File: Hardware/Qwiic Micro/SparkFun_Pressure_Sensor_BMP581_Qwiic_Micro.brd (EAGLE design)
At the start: 7.6 x 19.1 mm, 39 parts, among them J1 QWIIC_RIGHT_ANGLE, U1 BMP581

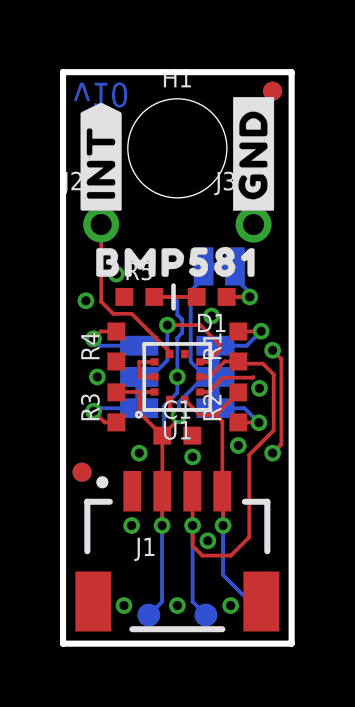
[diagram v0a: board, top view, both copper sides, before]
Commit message: Connect CSB of Micro board to VDD
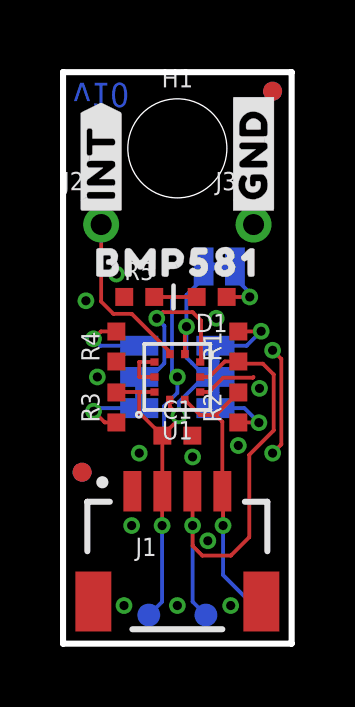
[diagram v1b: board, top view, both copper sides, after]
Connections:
- removed net !CSB!: U1.6
- net VDD: now also U1.6
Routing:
- net VDD: track 17.2 -> 18.2 mm, vias 2 -> 3
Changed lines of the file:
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@@
 <drawing>
 <settings>
-<setting alwaysvectorfont="yes"/>
+<setting alwaysvectorfont="no"/>
 <setting verticaltext="up"/>
 </settings>
@@
 <wire x1="5.08" y1="8.89" x2="4.699" y2="8.89" width="0.127" layer="16"/>
 <wire x1="5.08" y1="8.89" x2="4.759796875" y2="8.89" width="0.127" layer="16"/>
-<wire x1="4.759796875" y1="8.89" x2="4.2545" y2="9.39529375" width="0.127" layer="16"/>
-<wire x1="4.2545" y1="9.39529375" x2="4.2545" y2="11.7602" width="0.127" layer="16"/>
-<wire x1="4.6863" y1="12.192" x2="4.2545" y2="11.7602" width="0.127" layer="16"/>
+<wire x1="4.759796875" y1="8.89" x2="4.284896875" y2="9.364896875" width="0.127" layer="16"/>
 <wire x1="4.6863" y1="12.192" x2="4.6863" y2="12.573" width="0.127" layer="16"/>
+<via x="4.1148" y="10.5664" extent="1-16" drill="0.3048"/>
+<wire x1="4.06" y1="10.5116" x2="4.1148" y2="10.5664" width="0.127" layer="1"/>
+<wire x1="4.284896875" y1="9.364896875" x2="4.1148" y2="9.53499375" width="0.127" layer="16"/>
+<wire x1="4.1148" y1="9.53499375" x2="4.1148" y2="10.5664" width="0.127" layer="16"/>
+<wire x1="4.1148" y1="10.5664" x2="4.1148" y2="11.6205" width="0.127" layer="16"/>
+<wire x1="4.1148" y1="11.6205" x2="4.6863" y2="12.192" width="0.127" layer="16"/>
+<contactref element="U1" pad="6"/>
 <wire x1="3.0475" y1="8.39" x2="2.54" y2="8.39" width="0.127" layer="1"/>
 <wire x1="3.56" y1="8.1275" x2="3.56" y2="7.8954" width="0.127" layer="1"/>
+<wire x1="4.06" y1="9.6525" x2="4.06" y2="10.5116" width="0.127" layer="1"/>
 </signal>
 <signal name="GND">
@@
 <contactref element="C1" pad="2"/>
 <contactref element="R4" pad="1"/>
+<polygon width="0.254" layer="1" isolate="0.127">
+<vertex x="0" y="0"/>
+<vertex x="7.62" y="0"/>
+<vertex x="7.62" y="19.05"/>
+<vertex x="0" y="19.05"/>
+</polygon>
+<polygon width="0.254" layer="16" isolate="0.127">
+<vertex x="0" y="0"/>
+<vertex x="7.62" y="0"/>
+<vertex x="7.62" y="19.05"/>
+<vertex x="0" y="19.05"/>
+</polygon>
 <wire x1="1.0369" y1="0.9525" x2="0.9525" y2="0.9525" width="0.127" layer="16"/>
-<wire x1="2.54" y1="9.39" x2="2.54" y2="8.89" width="0.127" layer="1"/>
+<wire x1="2.54" y1="8.89" x2="2.54" y2="9.39" width="0.127" layer="1"/>
 <wire x1="6.3245" y1="8.8645" x2="6.35" y2="8.89" width="0.127" layer="1"/>
 <wire x1="4.86159375" y1="8.39" x2="5.33609375" y2="8.8645" width="0.127" layer="1"/>
@@
 <via x="0.762" y="11.43" extent="1-16" drill="0.3048"/>
 <via x="3.81" y="8.89" extent="1-16" drill="0.3048"/>
-<wire x1="3.81" y1="8.89" x2="3.81" y2="10.19404375" width="0.127" layer="16"/>
-<wire x1="3.81" y1="10.19404375" x2="3.9735" y2="10.35754375" width="0.127" layer="16"/>
-<wire x1="3.9735" y1="10.35754375" x2="3.9735" y2="10.80065625" width="0.127" layer="16"/>
-<wire x1="3.9735" y1="10.80065625" x2="3.81" y2="10.96415625" width="0.127" layer="16"/>
-<wire x1="3.81" y1="10.96415625" x2="3.81" y2="11.43" width="0.127" layer="16"/>
+<wire x1="3.81" y1="8.89" x2="3.6322" y2="9.0678" width="0.127" layer="16"/>
+<wire x1="3.6322" y1="11.4554" x2="3.6322" y2="9.0678" width="0.127" layer="16"/>
 <wire x1="3.81" y1="8.89" x2="3.81" y2="8.3602125" width="0.127" layer="16"/>
 <wire x1="3.3671" y1="7.0501" x2="3.302" y2="6.985" width="0.127" layer="16"/>
@@
 <via x="2.54" y="6.35" extent="1-16" drill="0.3048"/>
 <via x="1.143" y="8.89" extent="1-16" drill="0.3048"/>
-<via x="4.953" y="10.922" extent="1-16" drill="0.3048"/>
-<polygon width="0.254" layer="1" isolate="0.127">
-<vertex x="0" y="0"/>
-<vertex x="7.62" y="0"/>
-<vertex x="7.62" y="19.05"/>
-<vertex x="0" y="19.05"/>
-</polygon>
-<polygon width="0.254" layer="16" isolate="0.127">
-<vertex x="0" y="0"/>
-<vertex x="7.62" y="0"/>
-<vertex x="7.62" y="19.05"/>
-<vertex x="0" y="19.05"/>
-</polygon>
+<via x="5.1054" y="10.8458" extent="1-16" drill="0.3048"/>
 <wire x1="6.985" y1="6.35" x2="7.2771" y2="6.6421" width="0.127" layer="1"/>
 <wire x1="7.2771" y1="9.4869" x2="6.985" y2="9.779" width="0.127" layer="1"/>
 <wire x1="7.2771" y1="6.6421" x2="7.2771" y2="9.4869" width="0.127" layer="1"/>
+<wire x1="3.0475" y1="9.39" x2="2.54" y2="9.39" width="0.127" layer="1"/>
+<wire x1="3.0475" y1="8.89" x2="2.54" y2="8.89" width="0.127" layer="1"/>
 <wire x1="4.5725" y1="8.39" x2="4.86159375" y2="8.39" width="0.127" layer="1"/>
-<wire x1="3.0475" y1="8.89" x2="2.54" y2="8.89" width="0.127" layer="1"/>
-<wire x1="3.0475" y1="9.39" x2="2.54" y2="9.39" width="0.127" layer="1"/>
 </signal>
 <signal name="SDI/SDA">
@@
 <wire x1="5.334" y1="3.937" x2="5.334" y2="2.286" width="0.127" layer="16"/>
 <wire x1="5.334" y1="2.286" x2="6.6675" y2="0.9525" width="0.127" layer="16"/>
-<wire x1="4.06" y1="8.1275" x2="4.5675" y2="7.62" width="0.127" layer="1"/>
 <wire x1="4.5675" y1="7.62" x2="5.088" y2="7.62" width="0.127" layer="1"/>
+<wire x1="4.5675" y1="7.625" x2="4.5675" y2="7.62" width="0.127" layer="1"/>
+<wire x1="4.06" y1="8.1275" x2="4.5625" y2="7.625" width="0.127" layer="1"/>
+<wire x1="4.5625" y1="7.625" x2="4.5675" y2="7.625" width="0.127" layer="1"/>
 </signal>
 <signal name="SDO/ADR">
 <contactref element="U1" pad="5"/>
 <contactref element="JP1" pad="2"/>
-<via x="3.4798" y="10.6172" extent="1-16" drill="0.3048"/>
-<wire x1="3.4798" y1="10.6172" x2="4.572" y2="10.6172" width="0.127" layer="1"/>
-<wire x1="4.572" y1="10.6172" x2="5.207" y2="9.9822" width="0.127" layer="1"/>
-<wire x1="5.207" y1="9.9822" x2="5.207" y2="9.7755" width="0.127" layer="1"/>
-<wire x1="4.8215" y1="9.39" x2="5.207" y2="9.7755" width="0.127" layer="1"/>
+<via x="3.1242" y="10.8458" extent="1-16" drill="0.3048"/>
+<wire x1="3.1242" y1="10.8458" x2="3.3274" y2="11.049" width="0.127" layer="1"/>
+<wire x1="4.318" y1="11.049" x2="3.3274" y2="11.049" width="0.127" layer="1"/>
+<wire x1="4.5974" y1="10.7696" x2="4.318" y2="11.049" width="0.127" layer="1"/>
 <wire x1="2.54" y1="8.89" x2="2.921" y2="8.89" width="0.127" layer="16"/>
-<wire x1="2.921" y1="8.89" x2="3.4798" y2="9.4488" width="0.127" layer="16"/>
-<wire x1="3.4798" y1="9.4488" x2="3.4798" y2="10.6172" width="0.127" layer="16"/>
-<wire x1="4.5725" y1="9.39" x2="4.8215" y2="9.39" width="0.127" layer="1"/>
+<wire x1="2.921" y1="8.89" x2="3.3782" y2="9.3472" width="0.127" layer="16"/>
+<wire x1="3.3782" y1="10.5918" x2="3.1242" y2="10.8458" width="0.127" layer="16"/>
+<wire x1="3.3782" y1="10.5918" x2="3.3782" y2="9.3472" width="0.127" layer="16"/>
+<wire x1="4.5725" y1="9.39" x2="4.5974" y2="9.4149" width="0.127" layer="1"/>
+<wire x1="4.5974" y1="9.4149" x2="4.5974" y2="10.7696" width="0.127" layer="1"/>
 </signal>
 <signal name="INT">
@@
 <wire x1="3.56" y1="9.6525" x2="3.56" y2="9.7237" width="0.127" layer="1"/>
 </signal>
-<signal name="!CSB!">
-<contactref element="U1" pad="6"/>
-</signal>
 <signal name="N$5">

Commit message: Design review updates
Change INT label to fishtail in Micro silk
Add product name to bottom in 1x1 silk
Change Micro net labels to be I2C only
Approve DRC overlaps
Fix acid trap
Add note about CSB being tied high in Micro schematic
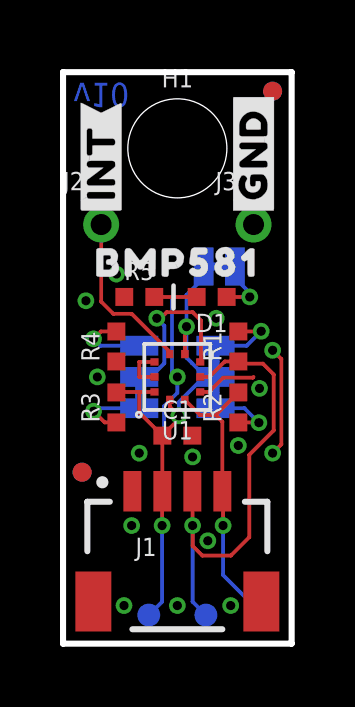
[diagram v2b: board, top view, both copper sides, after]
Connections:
- net SCK/SCL renamed SCL
- net SDI/SDA renamed SDA
- net SDO/ADR renamed ADR
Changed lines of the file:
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@@
 <drawing>
 <settings>
-<setting alwaysvectorfont="no"/>
+<setting alwaysvectorfont="yes"/>
 <setting verticaltext="up"/>
 </settings>
@@
 <wire x1="4.5725" y1="8.39" x2="4.86159375" y2="8.39" width="0.127" layer="1"/>
 </signal>
-<signal name="SDI/SDA">
+<signal name="SDA">
 <contactref element="U1" pad="4"/>
 <contactref element="J1" pad="3"/>
@@
 <wire x1="4.5725" y1="8.89" x2="4.87538125" y2="8.89" width="0.127" layer="1"/>
 </signal>
-<signal name="SCK/SCL">
+<signal name="SCL">
 <contactref element="U1" pad="2"/>
 <contactref element="J1" pad="4"/>
@@
 <wire x1="4.5625" y1="7.625" x2="4.5675" y2="7.625" width="0.127" layer="1"/>
 </signal>
-<signal name="SDO/ADR">
+<signal name="ADR">
 <contactref element="U1" pad="5"/>
 <contactref element="JP1" pad="2"/>
 <via x="3.1242" y="10.8458" extent="1-16" drill="0.3048"/>
-<wire x1="3.1242" y1="10.8458" x2="3.3274" y2="11.049" width="0.127" layer="1"/>
-<wire x1="4.318" y1="11.049" x2="3.3274" y2="11.049" width="0.127" layer="1"/>
+<wire x1="3.1242" y1="10.8458" x2="3.2512" y2="10.8458" width="0.127" layer="1"/>
+<wire x1="3.4544" y1="11.049" x2="3.2512" y2="10.8458" width="0.127" layer="1"/>
+<wire x1="4.318" y1="11.049" x2="3.4544" y2="11.049" width="0.127" layer="1"/>
 <wire x1="4.5974" y1="10.7696" x2="4.318" y2="11.049" width="0.127" layer="1"/>
 <wire x1="2.54" y1="8.89" x2="2.921" y2="8.89" width="0.127" layer="16"/>

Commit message: Remove library file
BMP384 is in SFE Eagle library, update part in design
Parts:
- U1: device BMP581:BMP581 -> SparkFun-Sensors:BMP581
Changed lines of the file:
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@@
 <element name="TP3" library="SparkFun-Connectors" package="PAD.03X.03" value="TEST-POINT3" x="4.7625" y="0.9525" smashed="yes" rot="MR0"/>
 <element name="TP4" library="SparkFun-Connectors" package="PAD.03X.03" value="TEST-POINT3" x="6.6675" y="0.9525" smashed="yes" rot="MR0"/>
-<element name="U1" library="BMP581" package="BMP581" value="BMP581" x="3.81" y="8.89" smashed="yes" rot="R180">
+<element name="U1" library="SparkFun-Sensors" package="BMP581" value="BMP581" x="3.81" y="8.89" smashed="yes" rot="R180">
 <attribute name="NAME" x="3.81" y="7.112" size="0.6096" layer="25" font="vector" ratio="20" rot="R180" align="center"/>
 <attribute name="PROD_ID" value="IC-16798" x="-11.43" y="27.94" size="1.778" layer="27" rot="R180" display="off"/>
